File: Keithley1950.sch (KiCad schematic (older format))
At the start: 73 parts

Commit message: Schematic work
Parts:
- removed C?: CP_Small, symbol Device:CP_Small
- removed U?: ULN2003, symbol Transistor_Array:ULN2003
- removed U?: 74HC595, symbol 74xx:74HC595
- added C12, C15: CTRIM_Small, symbol project:CTRIM_Small
- added C5, C6, C7: CP_Small, symbol Device:CP_Small
- added Q5, Q6: MMBT3906, Package_TO_SOT_SMD:SOT-23, symbol Transistor_BJT:MMBT3906
- added R1, R10, R13, R14, R2, R23: R_Small, symbol Device:R_Small
- added TP1, TP2, TP3: TestPoint, symbol Connector:TestPoint
- added U5: ULN2003, symbol project:ULN2003
- added U6: 74HC4094, symbol project:74HC4094
- gave numbers to parts that had none: 55
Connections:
- net labels added: +15V, +5V, -15V, 100R_EN, 1K_EN, AMPS_INP, CLOCK, DATA, DCAC-HI, GNDA, GNDS, INPUT_LO, RETURN, SHUNT_SIGNAL, SHUNT_TRMS_SW, SIGNAL_GUARD, SIGNAL_LO, SIGNAL_OUTPUT, STROBE, TRMS_DC_SIGNAL, TRMS_GAIN
- wire segments 0 -> 352
- no-connect marks 0 -> 7
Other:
- note added: "WHITE\nBLACK\nBLUE"
- note added: "YELLOW\nRED"
- moved on the sheet: C1, C10, C11, C13, C14, C2, C3, C4, C8, D1, D2, D3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

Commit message: More schematic work, put some values in
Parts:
- removed C8: CP_Small, symbol Device:CP_Small
- removed R15: R_Small, symbol Device:R_Small
- C1, C2, C3: value CP_Small -> 47uF; footprint (none) -> Capacitor_SMD:CP_Elec_6.3x5.2; Comment (none) -> 25v
- C10: value C_Small -> 610pF; footprint (none) -> Capacitor_SMD:C_0805_2012Metric
- C11: value C_Small -> 110pF; footprint (none) -> Capacitor_SMD:C_0805_2012Metric
- C12, C15: value CTRIM_Small -> 1.5pF; footprint (none) -> Capacitor_SMD:C_Trimmer_Murata_TZB4-A
- C13: value C_Small -> 15pF; footprint (none) -> Capacitor_SMD:C_0805_2012Metric
- C14: value C_Small -> 0.1uF; footprint (none) -> Capacitor_THT:C_Rect_L18.0mm_W5.0mm_P15.00mm_FKS3_FKP3; Comment (none) -> 1000v
- C4: value C_Small -> 470pF; footprint (none) -> Capacitor_SMD:C_0805_2012Metric
- D1, D2, D3, D4, D5, D6, D7: value D_Small -> S3M; footprint (none) -> Diode_SMD:D_SMC
- J1: footprint (none) -> Connector_IDC:IDC-Header_2x07_P2.54mm_Vertical
- J2: footprint (none) -> TerminalBlock_Phoenix:TerminalBlock_Phoenix_PT-1,5-3-5.0-H_1x03_P5.00mm_Horizontal
- J3: footprint (none) -> TerminalBlock_Phoenix:TerminalBlock_Phoenix_PT-1,5-2-5.0-H_1x02_P5.00mm_Horizontal
- Q1, Q2, Q3, Q4, Q7: value Q_NJFET_DGS -> MMBFJ111; footprint (none) -> Package_TO_SOT_SMD:SOT-23; symbol Device:Q_NJFET_DGS -> Device:Q_NJFET_DSG
- TP1, TP2, TP3: footprint (none) -> TestPoint:TestPoint_Pad_D2.5mm
- U1, U3, U7: footprint (none) -> Package_SO:SOIC-8_3.9x4.9mm_P1.27mm
- U4, U5, U6: footprint (none) -> Package_SO:SOIC-16_3.9x9.9mm_P1.27mm
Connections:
- net labels added: TRMS_GAIN_SW
- net labels removed: TRMS_GAIN
- wire segments 352 -> 353
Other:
- moved on the sheet: R3, R7

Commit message: Almost all components fully specified
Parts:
- removed K3: Relay_SP2P, symbol project:Relay_SP2P
- added C16, C8, C9: .1uF, Capacitor_SMD:C_0603_1608Metric, symbol Device:C_Small
- added K3: Relay_SP3P, Relay_THT:Relay_SPDT_SANYOU_SRD_Series_Form_C, symbol project:Relay_SP3P
- added unit 6 of U2
- C1, C2, C3: footprint Capacitor_SMD:CP_Elec_6.3x5.2 -> Capacitor_SMD:CP_Elec_6.3x5.9
- C12, C15: footprint Capacitor_SMD:C_Trimmer_Murata_TZB4-A -> Capacitor_SMD:C_Trimmer_Murata_TZB4-B
- C13: value 15pF -> 47pF
- K1, K2, K4, K5: footprint (none) -> Relay_THT:Relay_SPST_StandexMeder_SIL_Form1A
- K6, K7: footprint (none) -> Relay_THT:Relay_SPDT_SANYOU_SRD_Series_Form_C
- R1, R13, R14, R2, R23: value R_Small -> 10k; footprint (none) -> Resistor_SMD:R_0805_2012Metric
- R10: value R_Small -> 5R1; footprint (none) -> Resistor_SMD:R_2512_6332Metric
- R11: value R_Small -> 0R9; footprint (none) -> Resistor_SMD:R_2512_6332Metric; Comment (none) -> 0.1%
- R12: value R_Small -> 0R1; footprint (none) -> Resistor_SMD:R_2512_6332Metric; Comment (none) -> 0.1%
- R16: value R_Small -> 2k; footprint (none) -> Resistor_SMD:R_0805_2012Metric; Comment (none) -> 0.1%
- R17: value R_Small -> 27k; footprint (none) -> Resistor_SMD:R_0805_2012Metric; Comment (none) -> 0.1%
- R18: value R_Small -> 10k; footprint (none) -> Resistor_SMD:R_0805_2012Metric; Comment (none) -> 0.1%
- R19: value R_Small -> 24k; footprint (none) -> Resistor_SMD:R_0805_2012Metric
- R20: value R_Small -> 3k; footprint (none) -> Resistor_SMD:R_0805_2012Metric; Comment (none) -> 0.1%
- R21, R22: value R_Small -> 1M; footprint (none) -> Resistor_SMD:R_0805_2012Metric; Comment (none) -> 0.5%
- R24, R4, R5, R6, R9: value R_Small -> 100k; footprint (none) -> Resistor_SMD:R_0805_2012Metric
- R3: value R_Small -> 900R; footprint (none) -> Resistor_SMD:R_0805_2012Metric; Comment (none) -> 0.1%
- R7: value R_Small -> 90R; footprint (none) -> Resistor_SMD:R_0805_2012Metric; Comment (none) -> 0.1%
- R8: value R_Small -> 9R; footprint (none) -> Resistor_SMD:R_0805_2012Metric; Comment (none) -> 0.1%
- U2: footprint (none) -> Package_SO:SOIC-8_3.9x4.9mm_P1.27mm; symbol Comparator:LM339 -> project:LM339
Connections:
- net +5V: now also C16.2, C8.2, C9.2, K3.2
- net AMPS_INP: now also K3.3
- net GNDA: now also C16.1, C8.1, C9.1, U2.12 (V-)
- net at U5.12 (O5): now also K3.5
- net at R11.2, R12.1: now also K3.1
- no-connect marks 7 -> 8
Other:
- moved on the sheet: R1, R2, U2A, U2B, U2C, U2D

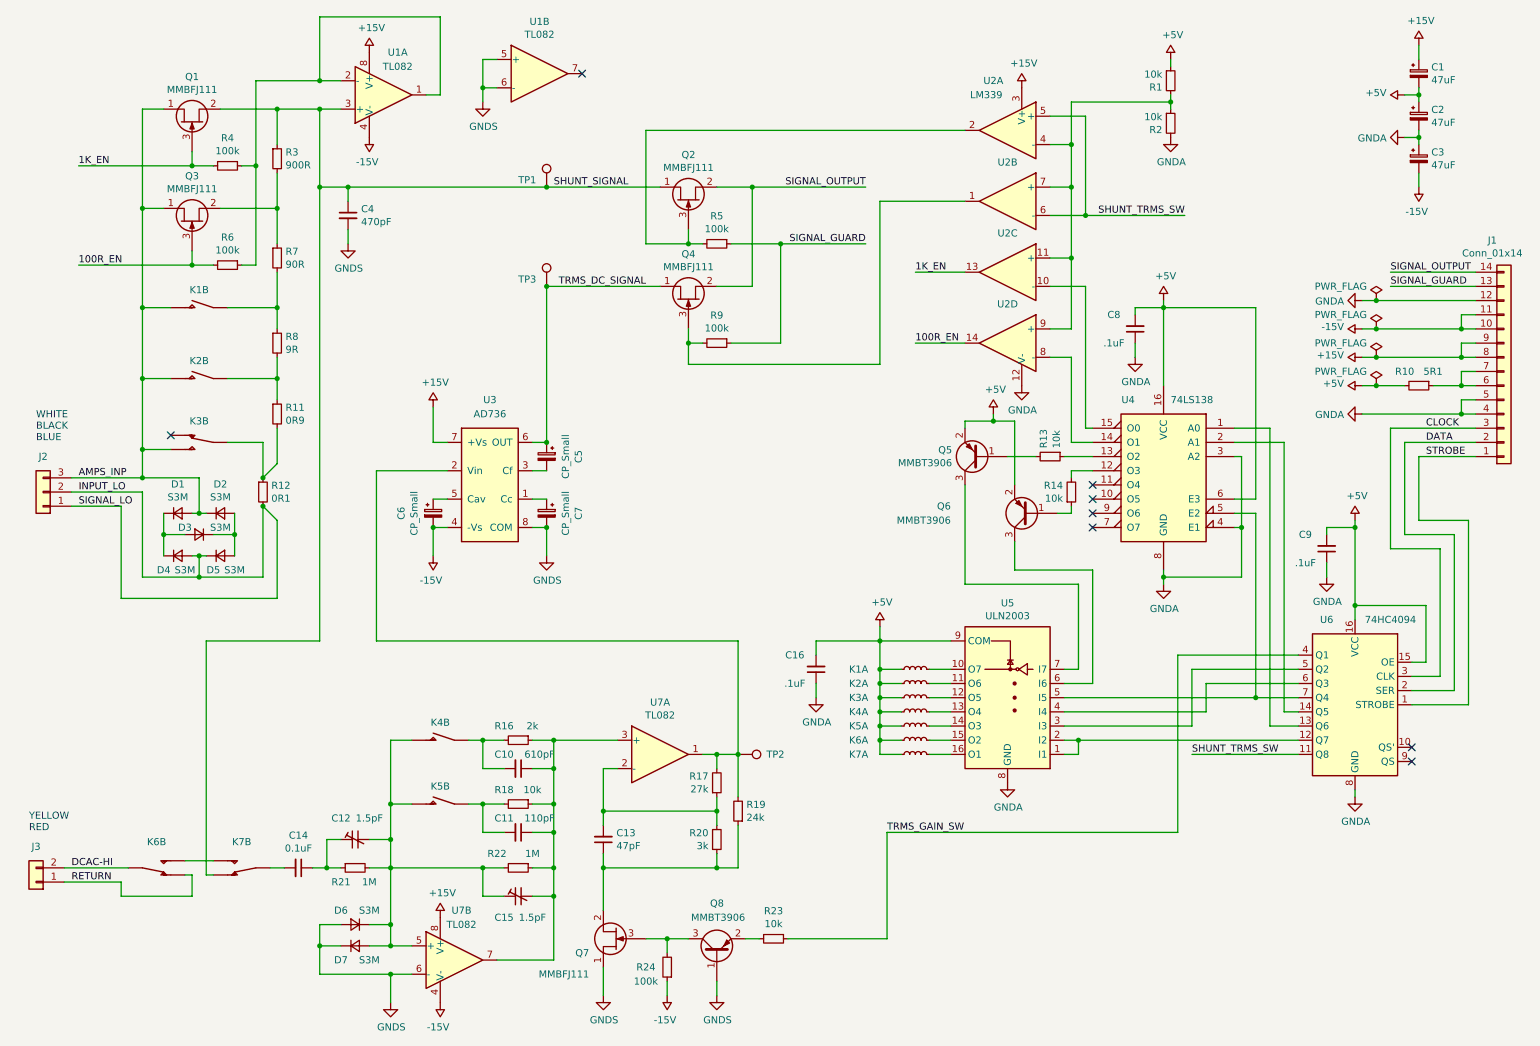
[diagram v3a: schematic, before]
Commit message: Switched to AD8436, finished schematic
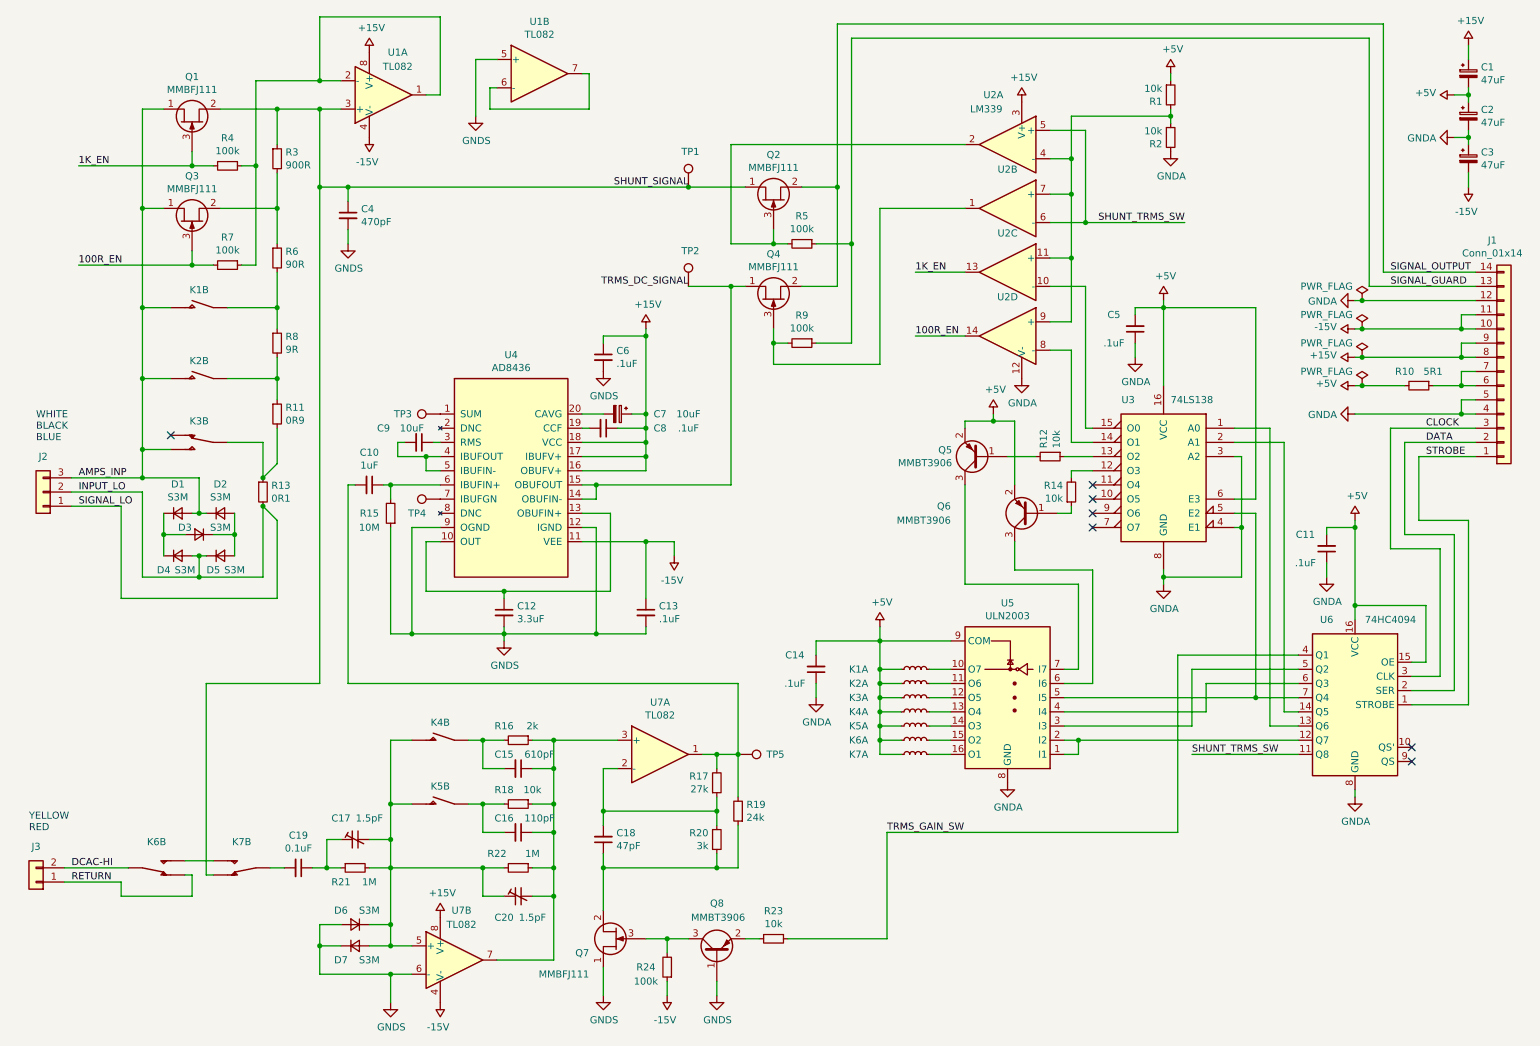
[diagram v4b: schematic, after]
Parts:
- removed C5, C6: CP_Small, symbol Device:CP_Small
- removed U3: AD736, Package_SO:SOIC-8_3.9x4.9mm_P1.27mm, symbol project:AD736
- added C10: 1uF, Capacitor_SMD:C_0805_2012Metric, symbol Device:C_Small
- added C12: 3.3uF, Capacitor_SMD:C_0603_1608Metric, symbol Device:C_Small
- added C13, C6, C8: .1uF, Capacitor_SMD:C_0603_1608Metric, symbol Device:C_Small
- added C9: 10uF, Capacitor_SMD:C_0805_2012Metric, symbol Device:C_Small
- added R15: 10M, Resistor_SMD:R_0805_2012Metric, symbol Device:R_Small
- added TP3, TP4: TestPoint, TestPoint:TestPoint_Pad_D2.5mm, symbol Connector:TestPoint
- added U4: AD8436, Package_SO:QSOP-20_3.9x8.7mm_P0.635mm, symbol project:AD8436
- C7: value CP_Small -> 10uF; footprint (none) -> Capacitor_SMD:CP_Elec_5x5.4
- R11: footprint Resistor_SMD:R_2512_6332Metric -> project:R_2512_x2_serial
- R13: renamed from R12; footprint Resistor_SMD:R_2512_6332Metric -> project:R_2512_With_10mm_axial
- R3: footprint Resistor_SMD:R_0805_2012Metric -> project:R_0805_x2_Serial
- R6: renamed from R7; footprint Resistor_SMD:R_0805_2012Metric -> project:R_0805_x2_Serial
- U2: footprint (none) -> Package_SO:SOIC-8_3.9x4.9mm_P1.27mm
- renumbered C9 to C11, C16 to C14, C10 to C15, C11 to C16, C12 to C17, C13 to C18, C14 to C19, C15 to C20, C8 to C5, R13 to R12, R6 to R7, TP3 to TP2, TP2 to TP5, U4 to U3
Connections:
- net +15V: now also C7.1, C6.1, C8.1, U4.16 (OBUFV+), U4.17 (IBUFV+), U4.18 (VCC)
- net -15V: now also C13.1, U4.11 (VEE)
- net GNDS: now also C12.2, C13.2, C6.2, R15.1, U4.12 (IGND), U4.9 (OGND); no longer C7.2, U1.6 (-)
- net TRMS_DC_SIGNAL: now also U4.14 (OBUFIN-), U4.15 (OBUFOUT)
- net at R17.2, R19.2, TP5.1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: now also C10.2
- net at U1.7: now also U1.6 (-)
- new net: TP3.1, U4.1 (SUM)
- new net: C12.1, U4.10 (OUT), U4.13 (OBUFIN+)
- new net: C8.2, U4.19 (CCF)
- new net: C7.2, U4.20 (CAVG)
- new net: C9.1, U4.3 (RMS)
- new net: C9.2, U4.4 (IBUFOUT), U4.5 (IBUFIN-)
- new net: C10.1, R15.2, U4.6 (IBUFIN+)
- new net: TP4.1, U4.7 (IBUFGN)
- no-connect marks 8 -> 7
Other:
- moved on the sheet: C1, C2, C3, Q2, Q4, R1, R2, R5, R9, TP1, TP2, U2A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
